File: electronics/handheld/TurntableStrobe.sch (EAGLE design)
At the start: 18 parts, among them IC1 TINY25, J1 ISP, Q1 12MHz

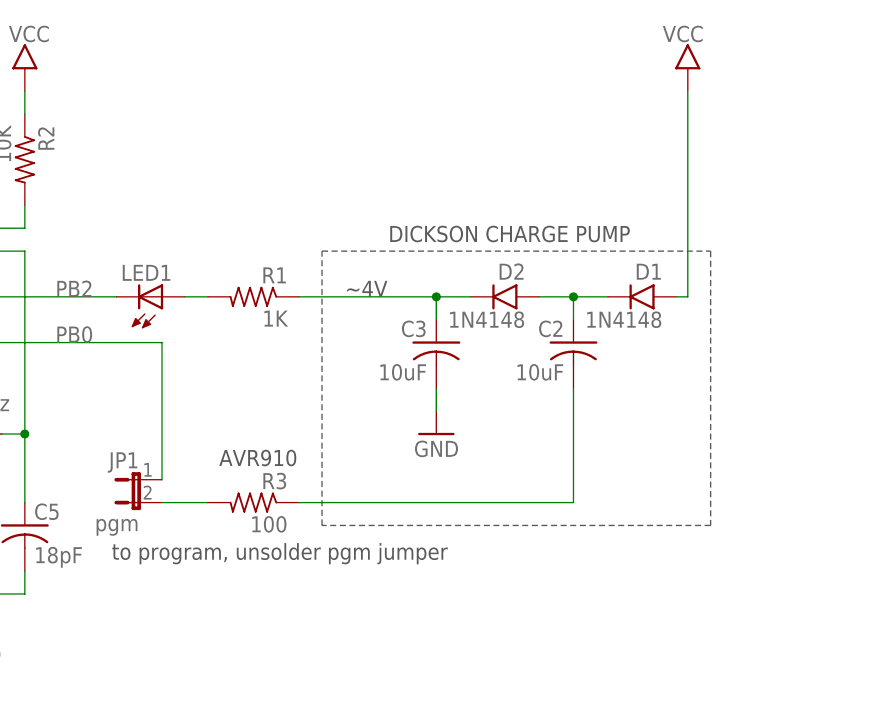
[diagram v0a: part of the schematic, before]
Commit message: diode array replaces discrete
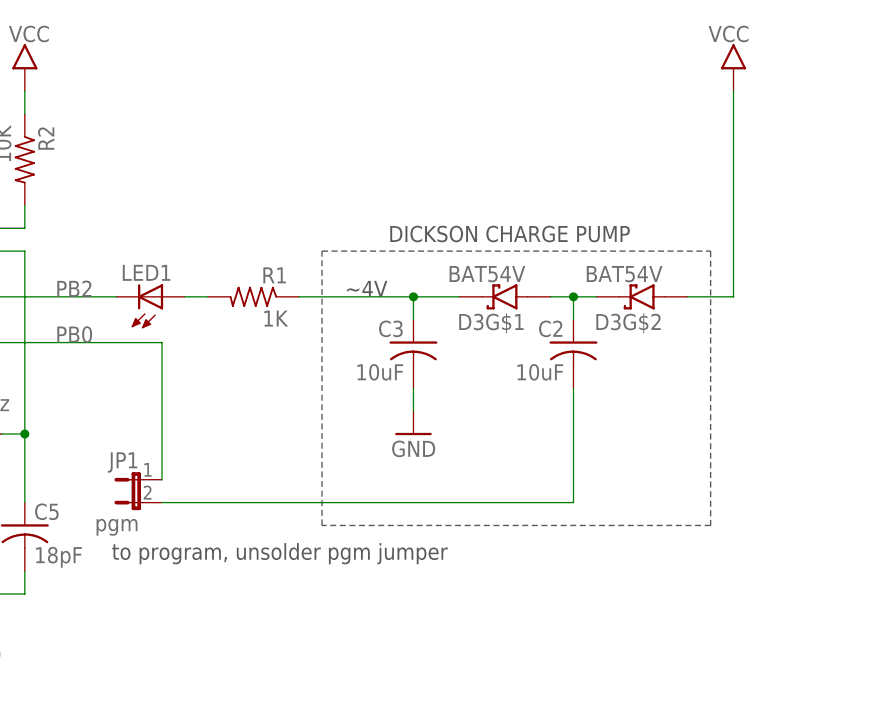
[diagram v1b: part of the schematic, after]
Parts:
- removed D1, D2: 1N4148, bt_diode:DIODE_SOD323
- removed R3: 100, rcl:R-US_R0603
- added D3: BAT54V, bt_diode:BAT54V
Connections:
- removed net N$1: JP1.2, R3.2
- net N$2: now also D3G$1.A, D3G$2.C; no longer D1.C, D2.A
- net N$4: now also JP1.2; no longer R3.1
- net VCC: now also D3G$2.A; no longer D1.A
- net VHI: now also D3G$1.C; no longer D2.C
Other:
- note removed: "AVR910"
- moved on the sheet: C3
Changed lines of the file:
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@@
 <part name="C2" library="rcl" deviceset="C-US" device="C0603" value="10uF"/>
 <part name="C3" library="rcl" deviceset="C-US" device="C0603" value="10uF"/>
-<part name="D1" library="bt_diode" deviceset="DIODE" device="_SOD323" value="1N4148"/>
-<part name="D2" library="bt_diode" deviceset="DIODE" device="_SOD323" value="1N4148"/>
 <part name="GND4" library="mes" deviceset="GND" device=""/>
 <part name="U$4" library="mes" deviceset="VCC" device="" value=""/>
-<part name="R3" library="rcl" deviceset="R-US_" device="R0603" value="100"/>
 <part name="JP1" library="SparkFun-Retired" deviceset="JUMPER-2" device="SMD-NO" value="pgm"/>
 <part name="U$5" library="bt" deviceset="BTLOGO" device="-LOGO-MD"/>
+<part name="D3" library="bt_diode" deviceset="BAT54V" device=""/>
 </parts>
 <sheets>
@@
 <wire x1="185.42" y1="91.44" x2="185.42" y2="121.92" width="0.1524" layer="97" style="shortdash"/>
 <text x="187.96" y="116.84" size="1.778" layer="97">~4V</text>
-<text x="173.99" y="98.044" size="1.778" layer="97">AVR910</text>
 <text x="150.876" y="17.78" size="3.81" layer="94">TURNTABLE STROBE</text>
 <text x="231.14" y="17.78" size="3.81" layer="94">R0.3</text>
@@
 <instance part="FRAME1" gate="G$2" x="147.32" y="2.54"/>
 <instance part="C2" gate="G$1" x="213.36" y="111.76" rot="MR0"/>
-<instance part="C3" gate="G$1" x="198.12" y="111.76" rot="MR0"/>
-<instance part="D1" gate="D1" x="220.98" y="116.84" rot="MR0"/>
-<instance part="D2" gate="D1" x="205.74" y="116.84" rot="MR0"/>
-<instance part="GND4" gate="1" x="198.12" y="101.6" rot="MR0"/>
-<instance part="U$4" gate="G$1" x="226.06" y="139.7" rot="MR0"/>
-<instance part="R3" gate="G$1" x="177.8" y="93.98" rot="MR0"/>
+<instance part="C3" gate="G$1" x="195.58" y="111.76" rot="MR0"/>
+<instance part="GND4" gate="1" x="195.58" y="101.6" rot="MR0"/>
+<instance part="U$4" gate="G$1" x="231.14" y="139.7" rot="MR0"/>
 <instance part="JP1" gate="A" x="165.1" y="96.52" rot="MR270"/>
 <instance part="U$5" gate="G$1" x="2.54" y="2.54"/>
+<instance part="D3" gate="G$1" x="205.74" y="116.84" rot="R180"/>
+<instance part="D3" gate="G$2" x="220.98" y="116.84" rot="R180"/>
 </instances>
 <busses>
@@
 </segment>
 <segment>
-<wire x1="224.79" y1="116.84" x2="226.06" y2="116.84" width="0.1524" layer="91"/>
-<wire x1="226.06" y1="116.84" x2="226.06" y2="139.7" width="0.1524" layer="91"/>
+<wire x1="226.06" y1="116.84" x2="231.14" y2="116.84" width="0.1524" layer="91"/>
+<wire x1="231.14" y1="116.84" x2="231.14" y2="139.7" width="0.1524" layer="91"/>
 <pinref part="U$4" gate="G$1" pin="VCC"/>
-<pinref part="D1" gate="D1" pin="A"/>
+<pinref part="D3" gate="G$2" pin="A"/>
 </segment>
 </net>
@@
 <pinref part="C3" gate="G$1" pin="2"/>
 <pinref part="GND4" gate="1" pin="GND"/>
-<wire x1="198.12" y1="104.14" x2="198.12" y2="106.68" width="0.1524" layer="91"/>
+<wire x1="195.58" y1="104.14" x2="195.58" y2="106.68" width="0.1524" layer="91"/>
 </segment>
 </net>
@@
 <segment>
 <pinref part="C3" gate="G$1" pin="1"/>
-<wire x1="198.12" y1="114.3" x2="198.12" y2="116.84" width="0.1524" layer="91"/>
-<pinref part="D2" gate="D1" pin="C"/>
-<wire x1="201.93" y1="116.84" x2="198.12" y2="116.84" width="0.1524" layer="91"/>
+<wire x1="195.58" y1="114.3" x2="195.58" y2="116.84" width="0.1524" layer="91"/>
 <pinref part="R1" gate="G$1" pin="1"/>
-<wire x1="198.12" y1="116.84" x2="182.88" y2="116.84" width="0.1524" layer="91"/>
-<junction x="198.12" y="116.84"/>
+<wire x1="200.66" y1="116.84" x2="195.58" y2="116.84" width="0.1524" layer="91"/>
+<wire x1="195.58" y1="116.84" x2="182.88" y2="116.84" width="0.1524" layer="91"/>
+<junction x="195.58" y="116.84"/>
+<pinref part="D3" gate="G$1" pin="C"/>
 </segment>
 </net>
@@
 <pinref part="C2" gate="G$1" pin="1"/>
 <wire x1="213.36" y1="114.3" x2="213.36" y2="116.84" width="0.1524" layer="91"/>
-<wire x1="213.36" y1="116.84" x2="217.17" y2="116.84" width="0.1524" layer="91"/>
-<pinref part="D1" gate="D1" pin="C"/>
-<pinref part="D2" gate="D1" pin="A"/>
-<wire x1="209.55" y1="116.84" x2="213.36" y2="116.84" width="0.1524" layer="91"/>
+<wire x1="213.36" y1="116.84" x2="215.9" y2="116.84" width="0.1524" layer="91"/>
 <junction x="213.36" y="116.84"/>
+<pinref part="D3" gate="G$1" pin="A"/>
+<wire x1="210.82" y1="116.84" x2="213.36" y2="116.84" width="0.1524" layer="91"/>
+<pinref part="D3" gate="G$2" pin="C"/>
 </segment>
 </net>
@@
 <pinref part="C2" gate="G$1" pin="2"/>
 <wire x1="213.36" y1="106.68" x2="213.36" y2="93.98" width="0.1524" layer="91"/>
-<pinref part="R3" gate="G$1" pin="1"/>
-<wire x1="182.88" y1="93.98" x2="213.36" y2="93.98" width="0.1524" layer="91"/>
-</segment>
-</net>
-<net name="N$1" class="0">
-<segment>
-<pinref part="R3" gate="G$1" pin="2"/>
+<wire x1="167.64" y1="93.98" x2="213.36" y2="93.98" width="0.1524" layer="91"/>
 <pinref part="JP1" gate="A" pin="2"/>
-<wire x1="167.64" y1="93.98" x2="172.72" y2="93.98" width="0.1524" layer="91"/>
-</segment>
-</net>
+</segment>
+</net>
